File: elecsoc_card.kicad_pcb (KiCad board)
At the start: 2 copper layers, 88 x 50 mm, 35 parts, among them J1 Conn_01x02_Pin, J2 Conn_01x02_Pin, U1 NA555D

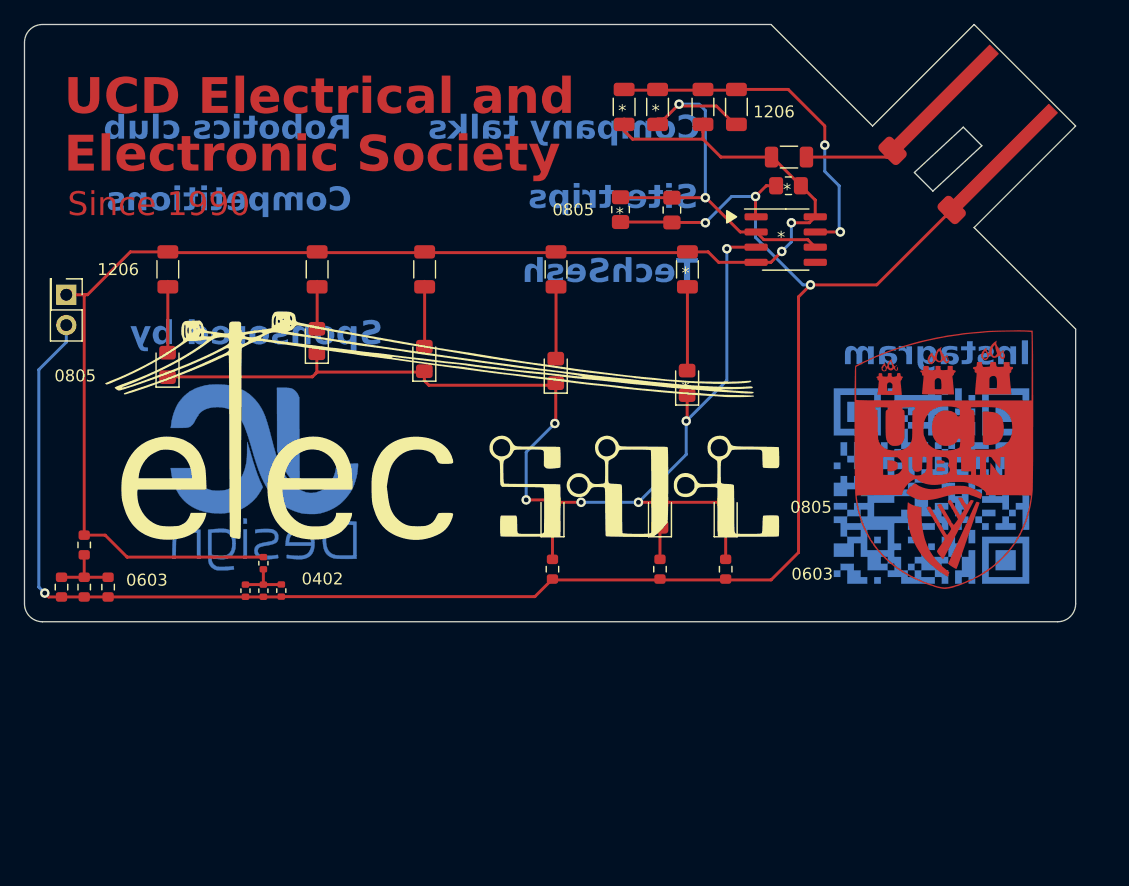
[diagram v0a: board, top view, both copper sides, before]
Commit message: Added soldering instructions
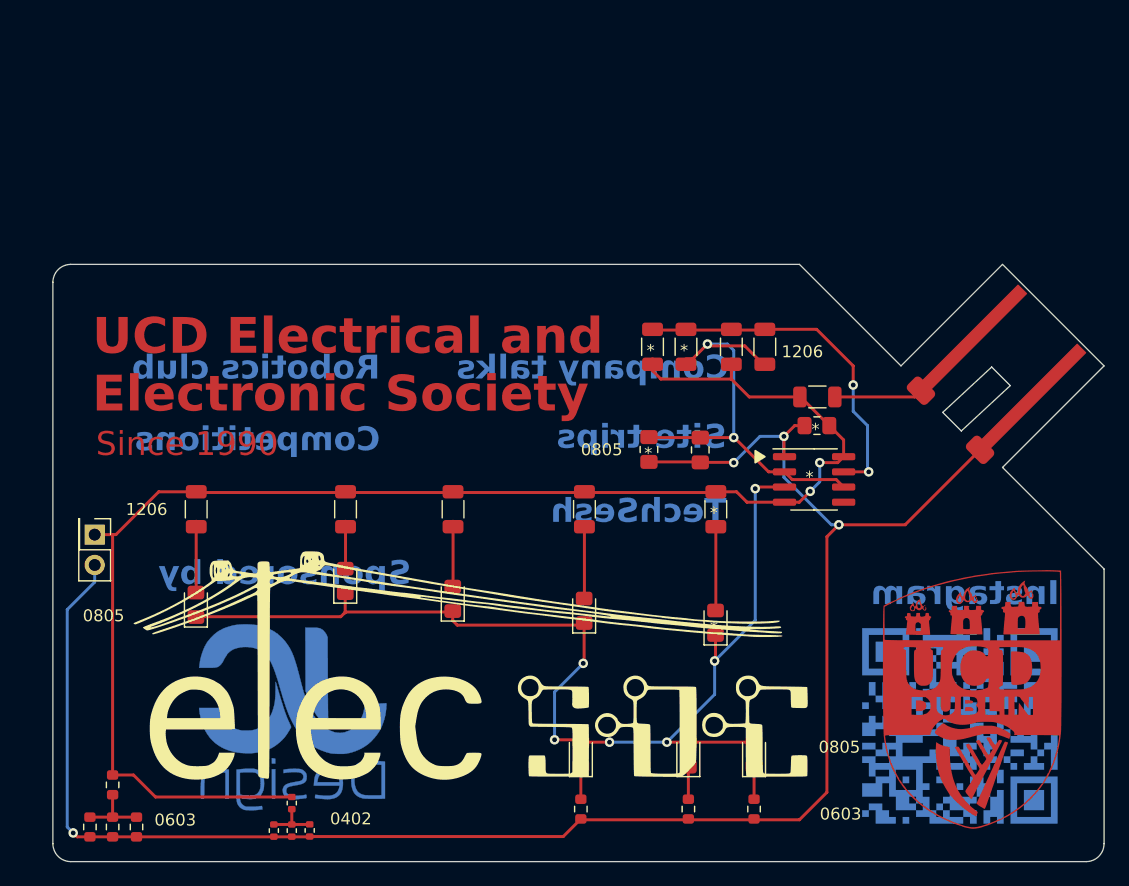
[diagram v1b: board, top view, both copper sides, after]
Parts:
- moved C3 20.2 mm to (156.6, 85.6)
- moved R10 20.2 mm to (161.1, 115.7)
- moved R13 20.2 mm to (109.4, 117.2)
- moved R14 20.2 mm to (105.5, 117.2)
- moved R15 20.2 mm to (107.4, 117.2)
- moved R17 20.2 mm to (122.4, 115.2)
- moved R8 20.2 mm to (146.6, 115.7)
- moved R9 20.2 mm to (155.6, 115.7)
- moved U1 20.2 mm to (166.1, 88.1)
- moved J1 20.2 mm to (177.5, 83.1)
- moved R1 20.2 mm to (152.6, 77.0)
- moved R18 20.2 mm to (162.0, 77.0)
- moved D1 20.2 mm to (157.9, 100.1)
- moved D2 20.2 mm to (146.9, 99.1)
- moved D3 20.2 mm to (135.9, 98.1)
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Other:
- outline, holes or cut-outs redrawn
